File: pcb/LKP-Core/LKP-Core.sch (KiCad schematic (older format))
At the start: 31 parts, among them J1 Intercon L, J2 Intercon R, J3 Power JST PH, J4 IO, J5 SWD, J6 WS281x, U1 CY8C4246AZI-M445

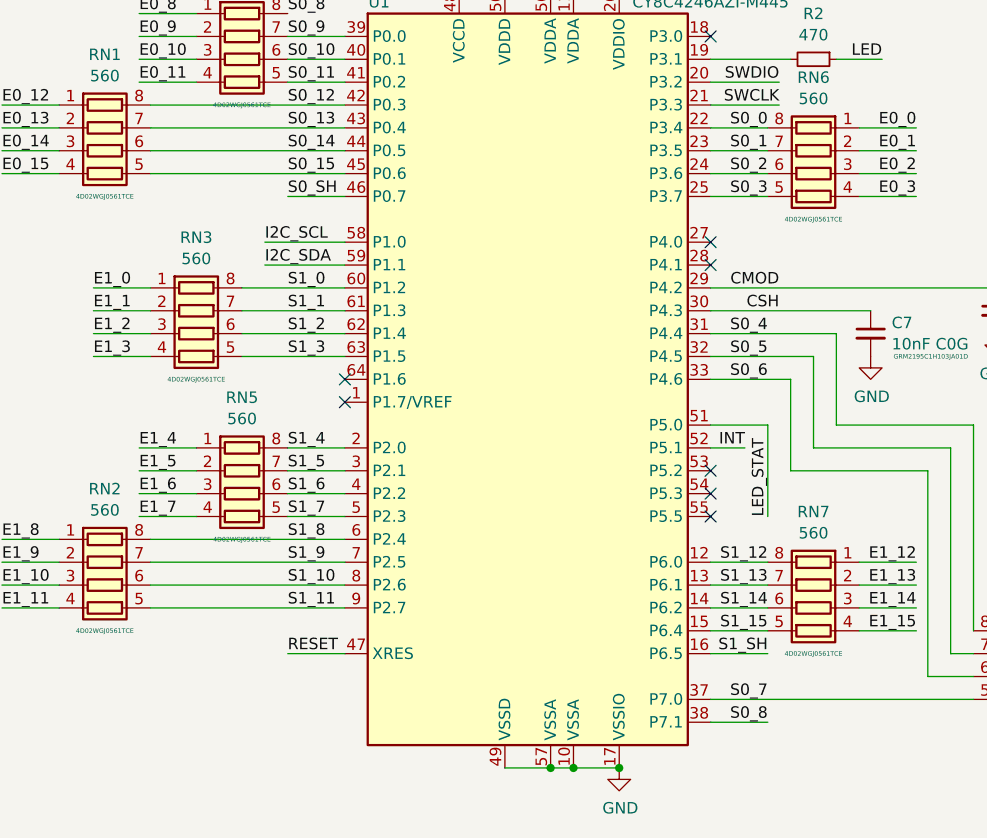
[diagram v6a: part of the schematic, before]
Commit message: Add resistors for shield
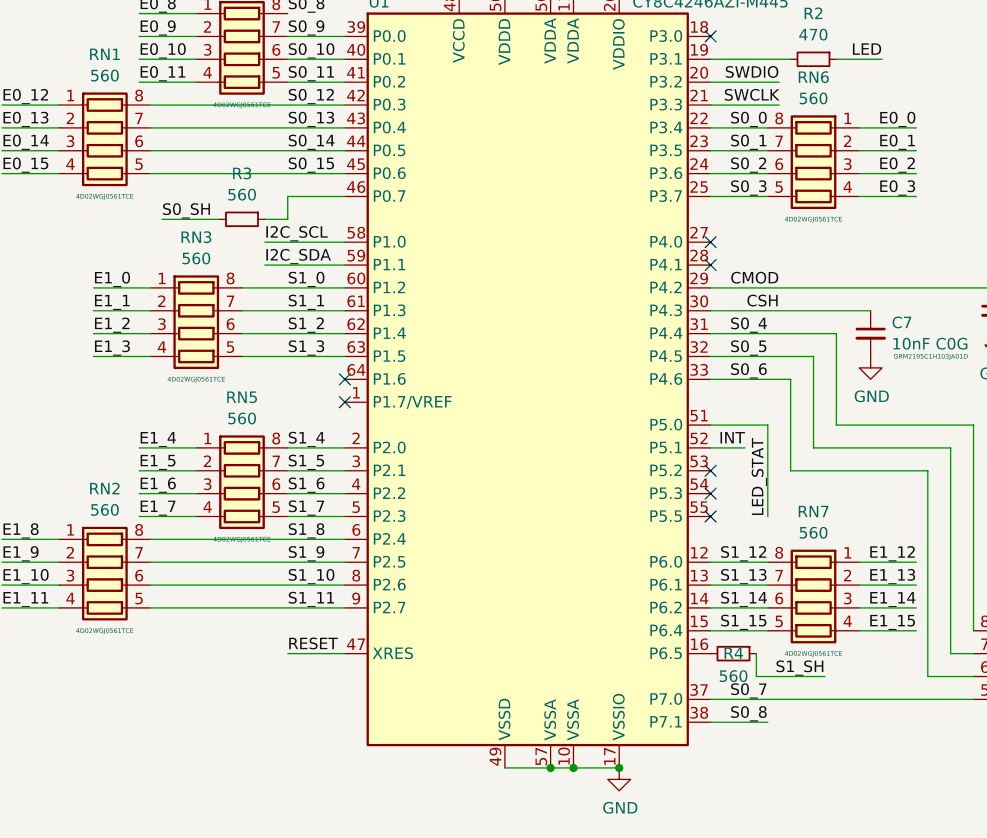
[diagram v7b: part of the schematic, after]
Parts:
- added R3, R4: 560, Resistor_SMD:R_0603_1608Metric, symbol Device:R_Small
- D2: footprint LED_SMD:LED_0805_2012Metric -> LED_SMD:LED_0805_2012Metric_Castellated
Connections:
- net S0_SH: now also R3.2; no longer U1.46 (P0.7)
- net S1_SH: now also R4.1; no longer U1.16 (P6.5)
- new net: R4.2, U1.16 (P6.5)
- new net: R3.1, U1.46 (P0.7)
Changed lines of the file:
@@
 Text Label 7350 4800 2    50   ~ 0
 E1_12
-Wire Wire Line
-	6700 5200 6450 5200
-Text Label 6700 5200 2    50   ~ 0
+Text Label 6950 5300 2    50   ~ 0
 S1_SH
 Text Label 6700 5400 2    50   ~ 0
@@
 Wire Wire Line
 	4850 2500 4600 2500
-Text Label 4600 3200 0    50   ~ 0
+Text Label 4050 3300 0    50   ~ 0
 S0_SH
 Text Label 4600 3100 0    50   ~ 0
@@
 F 0 "D2" H 8150 4690 50  0000 C CNN
 F 1 "Yellow" H 8150 4597 50  0000 C CNN
-F 2 "LED_SMD:LED_0805_2012Metric" V 8150 4450 50  0001 C CNN
+F 2 "LED_SMD:LED_0805_2012Metric_Castellated" V 8150 4450 50  0001 C CNN
 F 3 "~" V 8150 4450 50  0001 C CNN
 	1    8150 4450
 	1    0    0    -1
 $EndComp
+$Comp
+L Device:R_Small R4
+U 1 1 5D4F3AAE
+P 6550 5200
+F 0 "R4" V 6550 5200 50  0000 C CNN
+F 1 "560" V 6650 5200 50  0000 C CNN
+F 2 "Resistor_SMD:R_0603_1608Metric" H 6550 5200 50  0001 C CNN
+F 3 "~" H 6550 5200 50  0001 C CNN
+	1    6550 5200
+	0    1    1    0
+$EndComp
+Wire Wire Line
+	6650 5200 6650 5300
+Wire Wire Line
+	6650 5300 6950 5300
+$Comp
+L Device:R_Small R3
+U 1 1 5D508BD8
+P 4400 3300
+F 0 "R3" V 4201 3300 50  0000 C CNN
+F 1 "560" V 4294 3300 50  0000 C CNN
+F 2 "Resistor_SMD:R_0603_1608Metric" H 4400 3300 50  0001 C CNN
+F 3 "~" H 4400 3300 50  0001 C CNN
+	1    4400 3300
+	0    1    1    0
+$EndComp
+Wire Wire Line
+	4600 3200 4600 3300
+Wire Wire Line
+	4600 3300 4500 3300
+Wire Wire Line
+	4300 3300 4050 3300
 $EndSCHEMATC

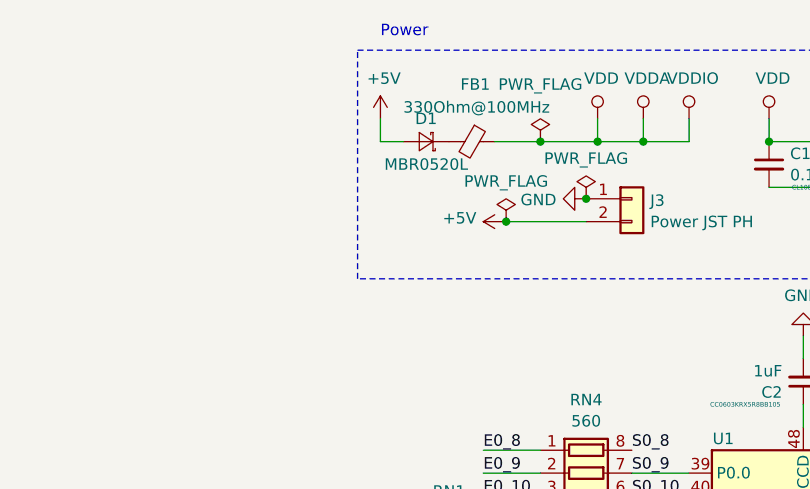
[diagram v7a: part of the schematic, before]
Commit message: Switch to through hole headers and add a capacitor for good luck
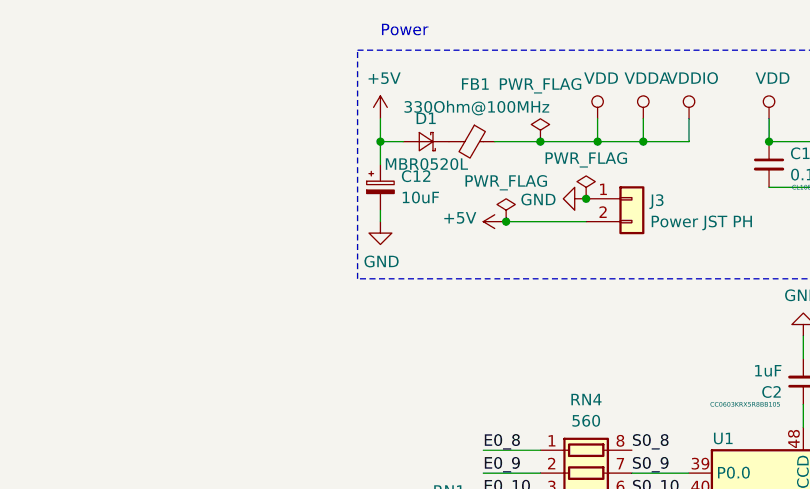
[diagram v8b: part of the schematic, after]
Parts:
- added C12: 10uF, Capacitor_Tantalum_SMD:CP_EIA-3216-18_Kemet-A, symbol Device:CP_Small
- J1, J2: footprint Connector_PinSocket_2.54mm:PinSocket_2x09_P2.54mm_Vertical_SMD -> Connector_PinSocket_2.54mm:PinSocket_2x09_P2.54mm_Vertical
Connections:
- net +5V: now also C12.1
- net GND: now also C12.2
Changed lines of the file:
@@
 F 0 "J1" H 1550 4320 50  0000 C CNN
 F 1 "Intercon L" H 1550 4227 50  0000 C CNN
-F 2 "Connector_PinSocket_2.54mm:PinSocket_2x09_P2.54mm_Vertical_SMD" H 1500 3700 50  0001 C CNN
+F 2 "Connector_PinSocket_2.54mm:PinSocket_2x09_P2.54mm_Vertical" H 1500 3700 50  0001 C CNN
 F 3 "~" H 1500 3700 50  0001 C CNN
 	1    1500 3700
@@
 F 0 "J2" H 2700 4320 50  0000 C CNN
 F 1 "Intercon R" H 2700 4227 50  0000 C CNN
-F 2 "Connector_PinSocket_2.54mm:PinSocket_2x09_P2.54mm_Vertical_SMD" H 2650 3700 50  0001 C CNN
+F 2 "Connector_PinSocket_2.54mm:PinSocket_2x09_P2.54mm_Vertical" H 2650 3700 50  0001 C CNN
 F 3 "~" H 2650 3700 50  0001 C CNN
 	1    2650 3700
@@
 Wire Wire Line
 	4300 3300 4050 3300
+$Comp
+L Device:CP_Small C12
+U 1 1 5D5BF537
+P 3500 1250
+F 0 "C12" H 3590 1297 50  0000 L CNN
+F 1 "10uF" H 3590 1204 50  0000 L CNN
+F 2 "Capacitor_Tantalum_SMD:CP_EIA-3216-18_Kemet-A" H 3500 1250 50  0001 C CNN
+F 3 "~" H 3500 1250 50  0001 C CNN
+	1    3500 1250
+	1    0    0    -1
+$EndComp
+Wire Wire Line
+	3500 1050 3500 1150
+Connection ~ 3500 1050
+$Comp
+L power:GND #PWR01
+U 1 1 5D5CE4B4
+P 3500 1400
+F 0 "#PWR01" H 3500 1150 50  0001 C CNN
+F 1 "GND" H 3505 1224 50  0000 C CNN
+F 2 "" H 3500 1400 50  0001 C CNN
+F 3 "" H 3500 1400 50  0001 C CNN
+	1    3500 1400
+	1    0    0    -1
+$EndComp
+Wire Wire Line
+	3500 1350 3500 1400
 $EndSCHEMATC
